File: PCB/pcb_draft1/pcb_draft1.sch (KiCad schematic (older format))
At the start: 51 parts

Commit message: Add footprints to most components (need to connect drivers)
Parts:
- removed Arduino-SolenoidControl: Conn_02x07_Counter_Clockwise, symbol Connector_Generic:Conn_02x07_Counter_Clockwise
- removed SolenoidOut: Conn_02x14_Counter_Clockwise, symbol Connector_Generic:Conn_02x14_Counter_Clockwise
- removed StepperOut: Conn_02x04_Counter_Clockwise, symbol Connector_Generic:Conn_02x04_Counter_Clockwise
- added Arduino-SolenoidControl1: Conn_02x07_Odd_Even, Connector_PinHeader_2.00mm:PinHeader_2x07_P2.00mm_Vertical, symbol Connector_Generic:Conn_02x07_Odd_Even
- added C1, C2: C, Capacitor_SMD:C_1206_3216Metric, symbol Device:C
- added SolenoidOut1: Conn_02x14_Odd_Even, Connector_PinHeader_2.00mm:PinHeader_2x14_P2.00mm_Vertical, symbol Connector_Generic:Conn_02x14_Odd_Even
- added StepperOut1: Conn_02x04_Odd_Even, Connector_PinHeader_2.00mm:PinHeader_2x04_P2.00mm_Vertical, symbol Connector_Generic:Conn_02x04_Odd_Even
- 12Vin1: renamed from 12Vin; footprint (none) -> Connector_PinHeader_2.00mm:PinHeader_1x02_P2.00mm_Vertical
- Arduino-StepperControl1: renamed from Arduino-StepperControl; footprint (none) -> Connector_PinHeader_2.00mm:PinHeader_1x07_P2.00mm_Vertical
- ArduinoPower1: renamed from ArduinoPower; footprint (none) -> Connector_PinHeader_2.00mm:PinHeader_1x03_P2.00mm_Vertical
- HomeSwitch1: renamed from HomeSwitch; footprint (none) -> Connector_PinHeader_2.00mm:PinHeader_1x02_P2.00mm_Vertical
- Q1, Q10, Q11, Q12, Q13, Q14, Q2, Q3, Q4, Q5, Q6, Q7, Q8, Q9: renamed from Q?; footprint Package_TO_SOT_SMD:SOT-23 -> Package_TO_SOT_SMD:SOT-223
- R1, R10, R11, R12, R13, R14, R2, R3, R4, R5, R6, R7, R8, R9: renamed from R?; footprint (none) -> Resistor_SMD:R_0603_1608Metric
- gave numbers to parts that had none: 16

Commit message: Add custom footprint for driver
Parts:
- U1, U2: footprint (none) -> custom_symbols:stepper_driver
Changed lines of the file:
@@
 F 0 "U2" H 3350 6065 50  0000 C CNN
 F 1 "STSPIN820" H 3350 5974 50  0000 C CNN
-F 2 "" H 3350 5000 50  0001 C CNN
+F 2 "custom_symbols:stepper_driver" H 3350 5000 50  0001 C CNN
 F 3 "" H 3350 5000 50  0001 C CNN
 	1    3150 5950
@@
 F 0 "U1" H 3350 4515 50  0000 C CNN
 F 1 "STSPIN820" H 3350 4424 50  0000 C CNN
-F 2 "" H 3350 3450 50  0001 C CNN
+F 2 "custom_symbols:stepper_driver" H 3350 3450 50  0001 C CNN
 F 3 "" H 3350 3450 50  0001 C CNN
 	1    3150 4400

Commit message: Add custom footprint for mosfet
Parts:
- Q1, Q10, Q11, Q12, Q13, Q14, Q2, Q3, Q4, Q5, Q6, Q7, Q8, Q9: footprint Package_TO_SOT_SMD:SOT-223 -> custom_symbols:SOT-223-edited
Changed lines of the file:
@@
 EESchema Schematic File Version 4
+LIBS:pcb_draft1-cache
 EELAYER 30 0
 EELAYER END
@@
 F 0 "Q14" H 8956 846 50  0000 L CNN
 F 1 "DMN6140L" H 8956 755 50  0000 L CNN
-F 2 "Package_TO_SOT_SMD:SOT-223" H 8950 725 50  0001 L CIN
+F 2 "custom_symbols:SOT-223-edited" H 8950 725 50  0001 L CIN
 F 3 "http://www.diodes.com/assets/Datasheets/DMN6140L.pdf" H 8750 800 50  0001 L CNN
 	1    8750 800
@@
 F 0 "Q7" H 8206 1196 50  0000 L CNN
 F 1 "DMN6140L" H 8206 1105 50  0000 L CNN
-F 2 "Package_TO_SOT_SMD:SOT-223" H 8200 1075 50  0001 L CIN
+F 2 "custom_symbols:SOT-223-edited" H 8200 1075 50  0001 L CIN
 F 3 "http://www.diodes.com/assets/Datasheets/DMN6140L.pdf" H 8000 1150 50  0001 L CNN
 	1    8000 1150
@@
 F 0 "Q11" H 8906 1696 50  0000 L CNN
 F 1 "DMN6140L" H 8906 1605 50  0000 L CNN
-F 2 "Package_TO_SOT_SMD:SOT-223" H 8900 1575 50  0001 L CIN
+F 2 "custom_symbols:SOT-223-edited" H 8900 1575 50  0001 L CIN
 F 3 "http://www.diodes.com/assets/Datasheets/DMN6140L.pdf" H 8700 1650 50  0001 L CNN
 	1    8700 1650
@@
 F 0 "Q4" H 8156 2046 50  0000 L CNN
 F 1 "DMN6140L" H 8156 1955 50  0000 L CNN
-F 2 "Package_TO_SOT_SMD:SOT-223" H 8150 1925 50  0001 L CIN
+F 2 "custom_symbols:SOT-223-edited" H 8150 1925 50  0001 L CIN
 F 3 "http://www.diodes.com/assets/Datasheets/DMN6140L.pdf" H 7950 2000 50  0001 L CNN
 	1    7950 2000
@@
 F 0 "Q12" H 8906 2546 50  0000 L CNN
 F 1 "DMN6140L" H 8906 2455 50  0000 L CNN
-F 2 "Package_TO_SOT_SMD:SOT-223" H 8900 2425 50  0001 L CIN
+F 2 "custom_symbols:SOT-223-edited" H 8900 2425 50  0001 L CIN
 F 3 "http://www.diodes.com/assets/Datasheets/DMN6140L.pdf" H 8700 2500 50  0001 L CNN
 	1    8700 2500
@@
 F 0 "Q5" H 8156 2896 50  0000 L CNN
 F 1 "DMN6140L" H 8156 2805 50  0000 L CNN
-F 2 "Package_TO_SOT_SMD:SOT-223" H 8150 2775 50  0001 L CIN
+F 2 "custom_symbols:SOT-223-edited" H 8150 2775 50  0001 L CIN
 F 3 "http://www.diodes.com/assets/Datasheets/DMN6140L.pdf" H 7950 2850 50  0001 L CNN
 	1    7950 2850
@@
 F 0 "Q13" H 8906 3396 50  0000 L CNN
 F 1 "DMN6140L" H 8906 3305 50  0000 L CNN
-F 2 "Package_TO_SOT_SMD:SOT-223" H 8900 3275 50  0001 L CIN
+F 2 "custom_symbols:SOT-223-edited" H 8900 3275 50  0001 L CIN
 F 3 "http://www.diodes.com/assets/Datasheets/DMN6140L.pdf" H 8700 3350 50  0001 L CNN
 	1    8700 3350
@@
 F 0 "Q6" H 8156 3746 50  0000 L CNN
 F 1 "DMN6140L" H 8156 3655 50  0000 L CNN
-F 2 "Package_TO_SOT_SMD:SOT-223" H 8150 3625 50  0001 L CIN
+F 2 "custom_symbols:SOT-223-edited" H 8150 3625 50  0001 L CIN
 F 3 "http://www.diodes.com/assets/Datasheets/DMN6140L.pdf" H 7950 3700 50  0001 L CNN
 	1    7950 3700
@@
 F 0 "Q10" H 8856 4246 50  0000 L CNN
 F 1 "DMN6140L" H 8856 4155 50  0000 L CNN
-F 2 "Package_TO_SOT_SMD:SOT-223" H 8850 4125 50  0001 L CIN
+F 2 "custom_symbols:SOT-223-edited" H 8850 4125 50  0001 L CIN
 F 3 "http://www.diodes.com/assets/Datasheets/DMN6140L.pdf" H 8650 4200 50  0001 L CNN
 	1    8650 4200
@@
 F 0 "Q3" H 8106 4596 50  0000 L CNN
 F 1 "DMN6140L" H 8106 4505 50  0000 L CNN
-F 2 "Package_TO_SOT_SMD:SOT-223" H 8100 4475 50  0001 L CIN
+F 2 "custom_symbols:SOT-223-edited" H 8100 4475 50  0001 L CIN
 F 3 "http://www.diodes.com/assets/Datasheets/DMN6140L.pdf" H 7900 4550 50  0001 L CNN
 	1    7900 4550
@@
 F 0 "Q8" H 8806 5096 50  0000 L CNN
 F 1 "DMN6140L" H 8806 5005 50  0000 L CNN
-F 2 "Package_TO_SOT_SMD:SOT-223" H 8800 4975 50  0001 L CIN
+F 2 "custom_symbols:SOT-223-edited" H 8800 4975 50  0001 L CIN
 F 3 "http://www.diodes.com/assets/Datasheets/DMN6140L.pdf" H 8600 5050 50  0001 L CNN
 	1    8600 5050
@@
 F 0 "Q1" H 8056 5446 50  0000 L CNN
 F 1 "DMN6140L" H 8056 5355 50  0000 L CNN
-F 2 "Package_TO_SOT_SMD:SOT-223" H 8050 5325 50  0001 L CIN
+F 2 "custom_symbols:SOT-223-edited" H 8050 5325 50  0001 L CIN
 F 3 "http://www.diodes.com/assets/Datasheets/DMN6140L.pdf" H 7850 5400 50  0001 L CNN
 	1    7850 5400
@@
 F 0 "Q9" H 8806 5946 50  0000 L CNN
 F 1 "DMN6140L" H 8806 5855 50  0000 L CNN
-F 2 "Package_TO_SOT_SMD:SOT-223" H 8800 5825 50  0001 L CIN
+F 2 "custom_symbols:SOT-223-edited" H 8800 5825 50  0001 L CIN
 F 3 "http://www.diodes.com/assets/Datasheets/DMN6140L.pdf" H 8600 5900 50  0001 L CNN
 	1    8600 5900
@@
 F 0 "Q2" H 8056 6296 50  0000 L CNN
 F 1 "DMN6140L" H 8056 6205 50  0000 L CNN
-F 2 "Package_TO_SOT_SMD:SOT-223" H 8050 6175 50  0001 L CIN
+F 2 "custom_symbols:SOT-223-edited" H 8050 6175 50  0001 L CIN
 F 3 "http://www.diodes.com/assets/Datasheets/DMN6140L.pdf" H 7850 6250 50  0001 L CNN
 	1    7850 6250

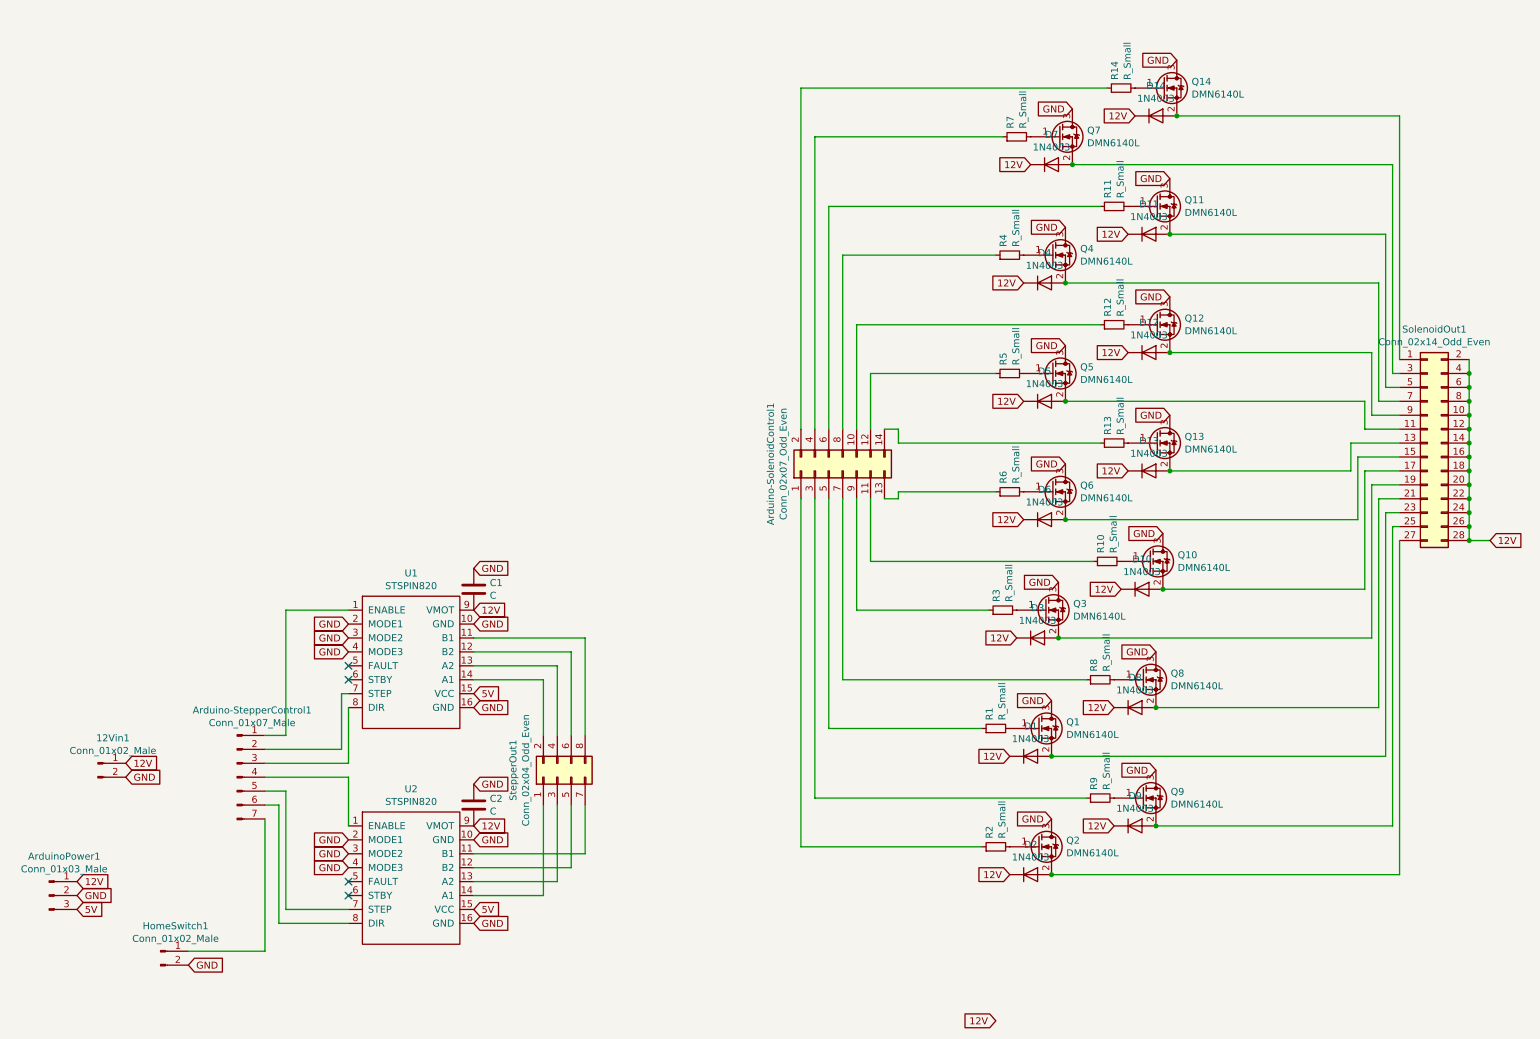
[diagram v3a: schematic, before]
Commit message: Update PCB to add fan and thermistor (needs to be fixed)
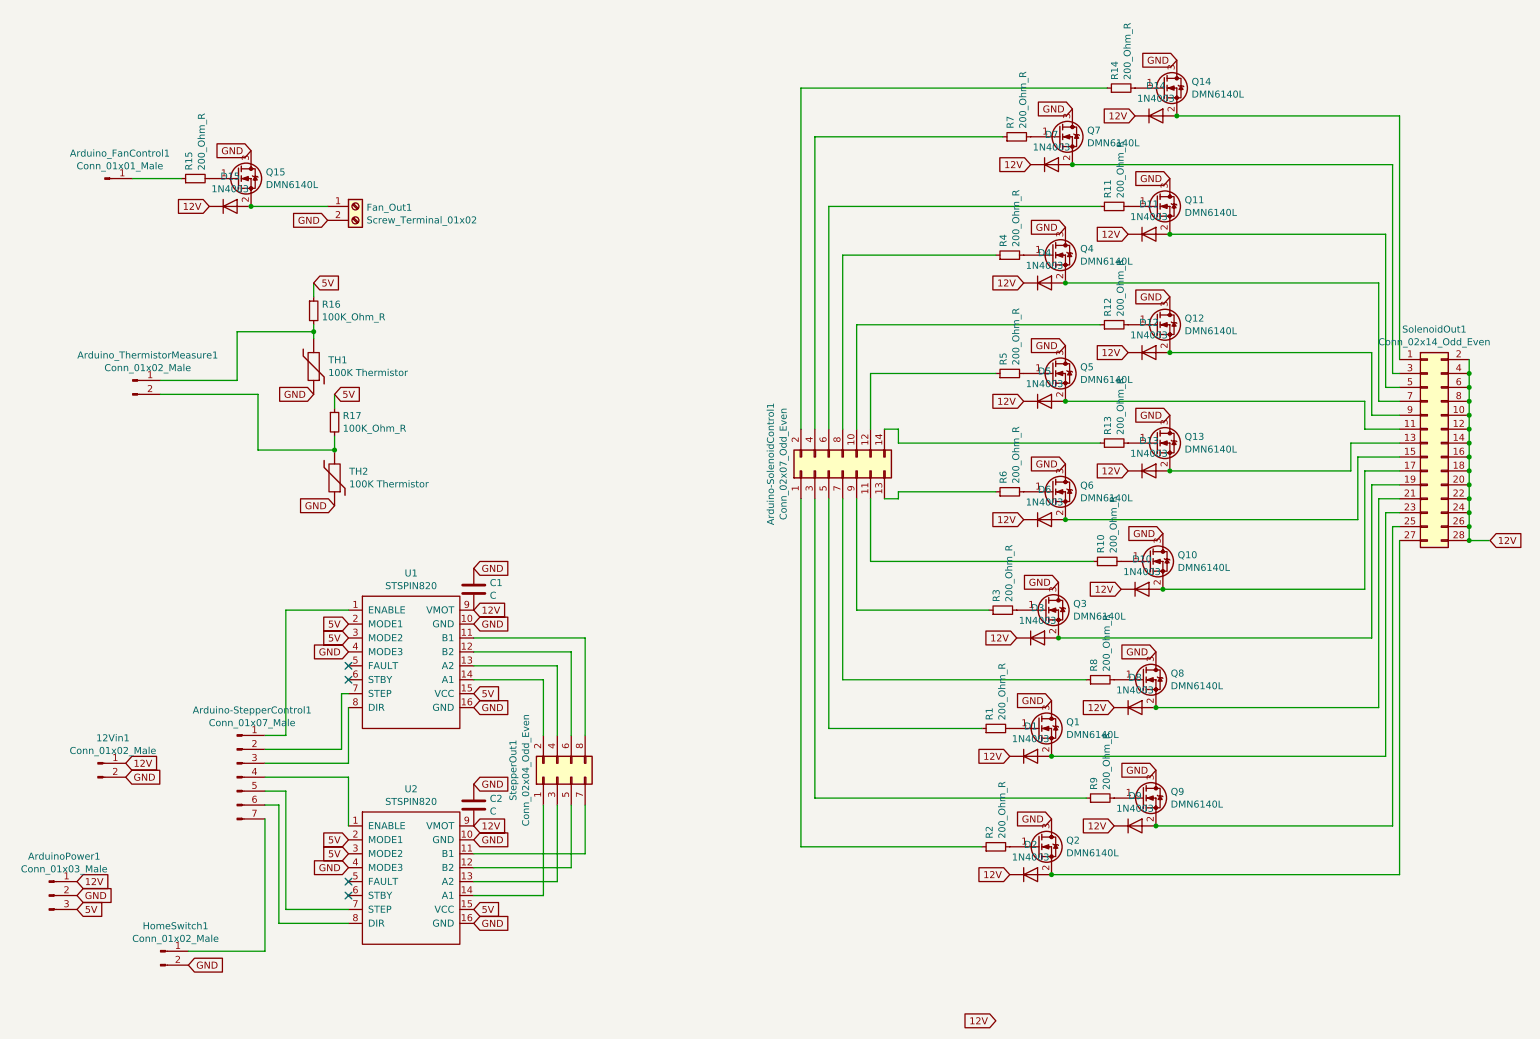
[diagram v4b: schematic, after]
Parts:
- added Arduino_FanControl1: Conn_01x01_Male, Connector_PinHeader_2.54mm:PinHeader_1x01_P2.54mm_Vertical, symbol Connector:Conn_01x01_Male
- added Arduino_ThermistorMeasure1: Conn_01x02_Male, symbol Connector:Conn_01x02_Male
- added D15: 1N4003, Diode_THT:D_DO-41_SOD81_P10.16mm_Horizontal, symbol Diode:1N4003
- added Fan_Out1: Screw_Terminal_01x02, TerminalBlock_Phoenix:TerminalBlock_Phoenix_MKDS-1,5-2_1x02_P5.00mm_Horizontal, symbol Connector:Screw_Terminal_01x02
- added Q15: DMN6140L, custom_symbols:SOT-223-edited, symbol Transistor_FET:DMN6140L
- added R15: 200_Ohm_R, Resistor_SMD:R_0603_1608Metric, symbol Device:R_Small
- added R16, R17: 100K_Ohm_R, symbol Device:R_Small
- added TH1, TH2: 100K Thermistor, symbol Device:Thermistor
- 12Vin1, HomeSwitch1: footprint Connector_PinHeader_2.00mm:PinHeader_1x02_P2.00mm_Vertical -> Connector_PinHeader_2.54mm:PinHeader_1x02_P2.54mm_Vertical
- Arduino-SolenoidControl1: footprint Connector_PinHeader_2.00mm:PinHeader_2x07_P2.00mm_Vertical -> Connector_PinHeader_2.54mm:PinHeader_2x07_P2.54mm_Vertical
- Arduino-StepperControl1: footprint Connector_PinHeader_2.00mm:PinHeader_1x07_P2.00mm_Vertical -> Connector_PinHeader_2.54mm:PinHeader_1x07_P2.54mm_Vertical
- ArduinoPower1: footprint Connector_PinHeader_2.00mm:PinHeader_1x03_P2.00mm_Vertical -> Connector_PinHeader_2.54mm:PinHeader_1x03_P2.54mm_Vertical
- R1, R10, R11, R12, R13, R14, R2, R3, R4, R5, R6, R7, R8, R9: value R_Small -> 200_Ohm_R
- SolenoidOut1: footprint Connector_PinHeader_2.00mm:PinHeader_2x14_P2.00mm_Vertical -> Connector_PinHeader_2.54mm:PinHeader_2x14_P2.54mm_Vertical
- StepperOut1: footprint Connector_PinHeader_2.00mm:PinHeader_2x04_P2.00mm_Vertical -> Connector_PinHeader_2.54mm:PinHeader_2x04_P2.54mm_Vertical
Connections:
- net 12V: now also D15.1 (K)
- net 5V: now also U1.2 (MODE1), U1.3 (MODE2), U2.2 (MODE1), U2.3 (MODE2), R16.1, R17.1
- net GND: now also Fan_Out1.2 (Pin_2), Q15.3 (D), TH1.1, TH2.1; no longer U1.2 (MODE1), U1.3 (MODE2), U2.2 (MODE1), U2.3 (MODE2)
- new net: D15.2 (A), Fan_Out1.1 (Pin_1), Q15.2 (S)
- new net: Q15.1 (G), R15.2
- new net: Arduino_FanControl1.1 (Pin_1), R15.1
- new net: Arduino_ThermistorMeasure1.1 (Pin_1), R16.2, TH1.2
- new net: Arduino_ThermistorMeasure1.2 (Pin_2), R17.2, TH2.2

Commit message: Update PCB
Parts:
- Arduino_ThermistorMeasure1: footprint (none) -> Connector_PinHeader_2.54mm:PinHeader_1x02_P2.54mm_Vertical
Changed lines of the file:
@@
 F 0 "Arduino_ThermistorMeasure1" H 1458 3081 50  0000 C CNN
 F 1 "Conn_01x02_Male" H 1458 2990 50  0000 C CNN
-F 2 "" H 1350 2900 50  0001 C CNN
+F 2 "Connector_PinHeader_2.54mm:PinHeader_1x02_P2.54mm_Vertical" H 1350 2900 50  0001 C CNN
 F 3 "~" H 1350 2900 50  0001 C CNN
 	1    1350 2900
